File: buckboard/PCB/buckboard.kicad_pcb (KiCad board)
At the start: 2 copper layers, 387.6 x 194.6 mm, 159 parts, among them J1 Conn_01x05, SW1 SW_Push, SW10 SW_Push, SW100_1.25 SW_Push, SW101 SW_Push, SW102 SW_Push, SW103_1.25 SW_Push, SW104_1.25 SW_Push, SW105_1.25 SW_Push, SW106_1.5 SW_Push, SW11 SW_Push, SW12 SW_Push, SW13 SW_Push, SW17 SW_Push, SW18 SW_Push, SW19 SW_Push, SW2 SW_Push, SW20 SW_Push, SW21 SW_Push, SW22 SW_Push, SW23 SW_Push, SW24 SW_Push, SW25 SW_Push, SW26 SW_Push, SW27 SW_Push, SW28 SW_Push, SW29 SW_Push, SW3 SW_Push, SW30_2 SW_Push, SW4 SW_Push, SW5 SW_Push, SW58_1.5 SW_Push, SW59 SW_Push, SW6 SW_Push, SW60 SW_Push, SW61 SW_Push, SW62 SW_Push, SW63 SW_Push, SW64 SW_Push, SW65 SW_Push, SW66 SW_Push, SW67 SW_Push, SW68 SW_Push, SW69 SW_Push, SW7 SW_Push, SW70 SW_Push, SW71 SW_Push, SW71_1.75 SW_Push, SW72 SW_Push, SW73 SW_Push, SW74 SW_Push, SW75 SW_Push, SW76 SW_Push, SW77 SW_Push, SW78 SW_Push, SW79 SW_Push, SW8 SW_Push, SW80 SW_Push, SW81 SW_Push, SW82 SW_Push, SW83 SW_Push, SW84_enter1 SW_Push, SW85_1.25 SW_Push, SW86 SW_Push, SW87 SW_Push, SW88 SW_Push, SW89 SW_Push, SW9 SW_Push, SW90 SW_Push, SW91 SW_Push, SW92 SW_Push, SW93 SW_Push, SW94 SW_Push, SW95 SW_Push, SW96 SW_Push, SW97_2.75 SW_Push, SW98_1.5 SW_Push, SW99_1.25 SW_Push

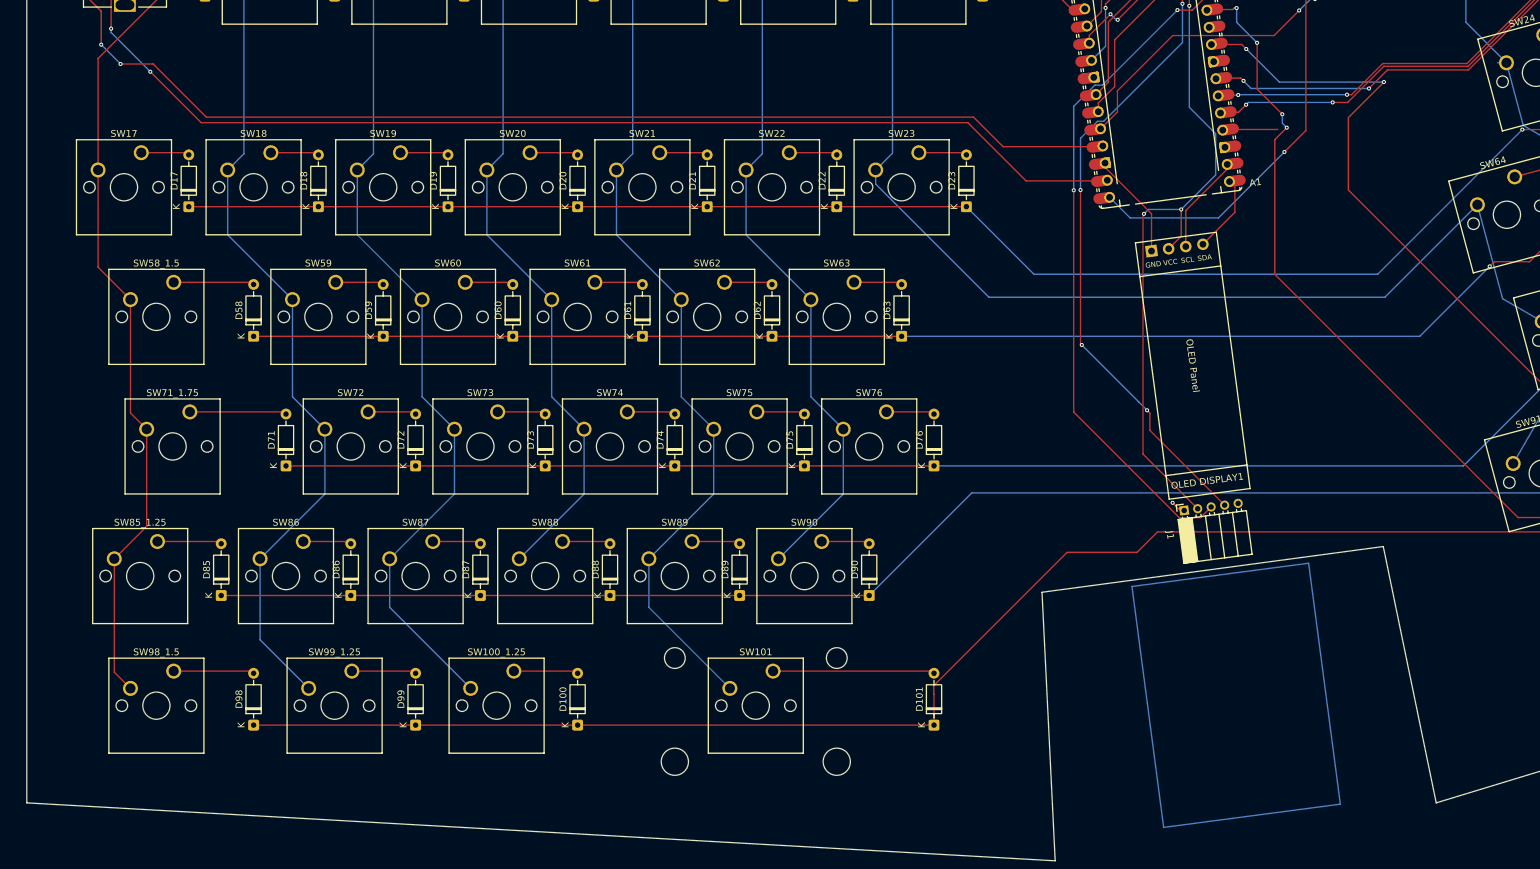
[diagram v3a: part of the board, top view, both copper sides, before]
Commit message: made working firmware for the board (joysytick still unsupported)
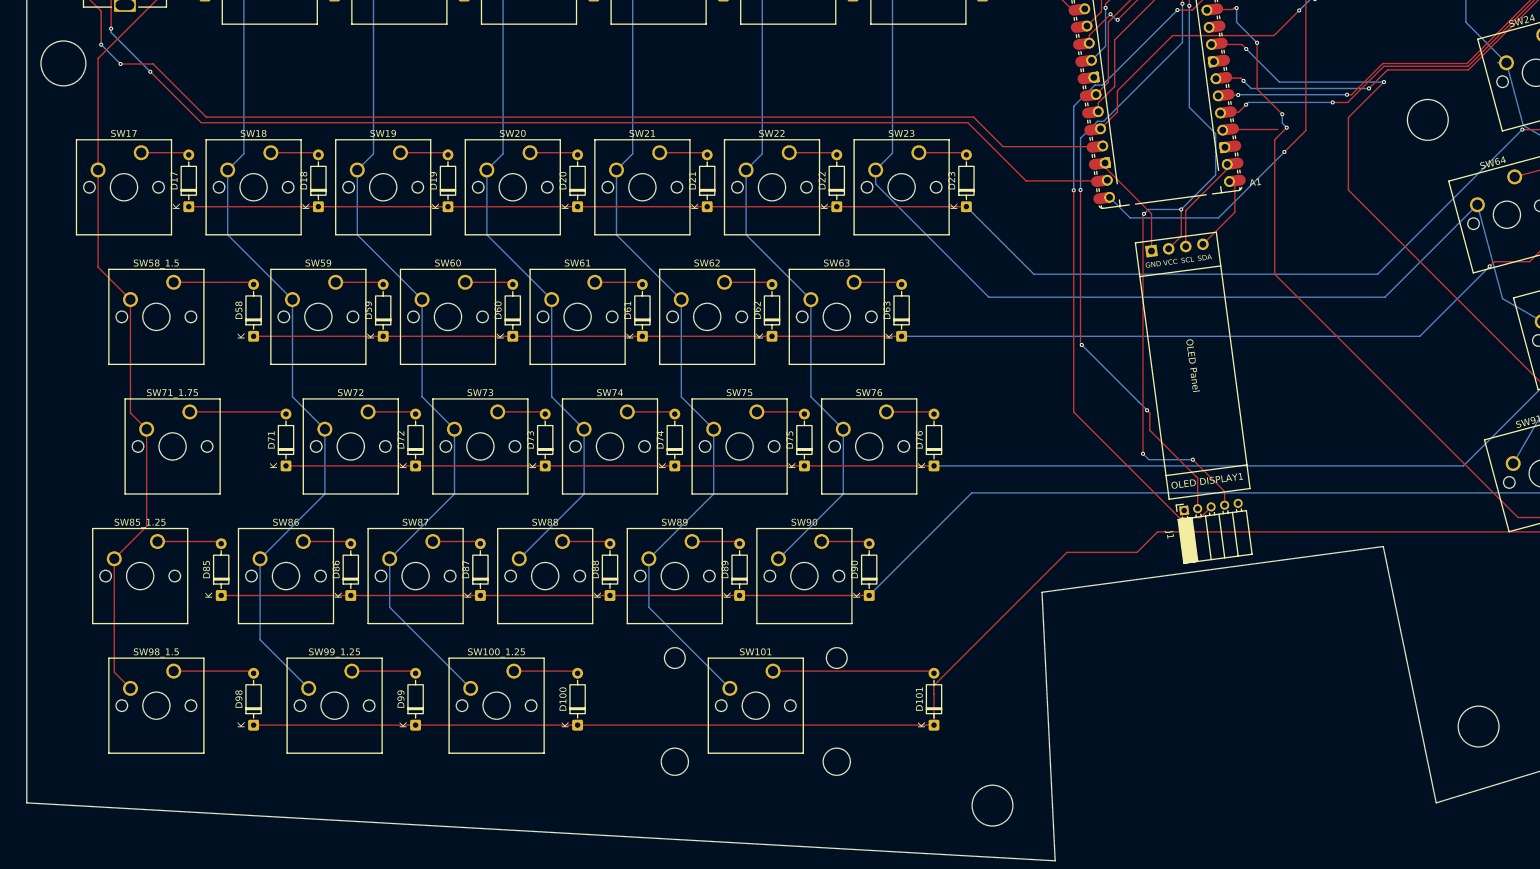
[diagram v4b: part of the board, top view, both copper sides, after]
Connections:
- J1 pad 1: GND -> JSW
- J1 pad 2: +3.3V -> VRy
- J1 pad 4: VRy -> +3.3V
- J1 pad 5: JSW -> GND
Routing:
- net +3.3V: track 109.6 -> 114.6 mm, vias 4 -> 6
- net GND: track 17.9 -> 15.8 mm, vias 1 -> 0
- net VRy: track 99.8 -> 98.6 mm
- net JSW: track 0.00 -> 0.57 mm
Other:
- outline, holes or cut-outs redrawn
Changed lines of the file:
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@@
 			(layers "*.Cu" "*.Mask")
 			(remove_unused_layers no)
-			(net "GND")
+			(net "JSW")
 			(pinfunction "Pin_1_1")
 			(pintype "passive")
@@
 			(layers "*.Cu" "*.Mask")
 			(remove_unused_layers no)
-			(net "+3.3V")
+			(net "VRy")
 			(pinfunction "Pin_2_2")
 			(pintype "passive")
@@
 			(layers "*.Cu" "*.Mask")
 			(remove_unused_layers no)
-			(net "VRy")
+			(net "+3.3V")
 			(pinfunction "Pin_4_4")
 			(pintype "passive")
@@
 			(layers "*.Cu" "*.Mask")
 			(remove_unused_layers no)
-			(net "JSW")
+			(net "GND")
 			(pinfunction "Pin_5_5")
 			(pintype "passive")
@@
 			)
 		)
+		(model "C:/Users/marin/Downloads/REDragon-MX-ZT02.stp"
+			(offset
+				(xyz -2.5 -5 0)
+			)
+			(scale
+				(xyz 1 1 1)
+			)
+			(rotate
+				(xyz -0 -0 -0)
+			)
+		)
 	)
 	(footprint "Button_Switch_Keyboard:SW_Cherry_MX_1.00u_PCB"
@@
 	(gr_poly
 		(pts
-			(xy 586.306444 230.131403) (xy 612.276103 226.712432) (xy 616.938335 262.125603) (xy 590.968676 265.544574)
+			(xy 811.498592 206.993148) (xy 631.03125 261.9375) (xy 623.25 224.26) (xy 573.088052 230.98125) (xy 575.023056 270.453588)
+			(xy 423.8625 261.9375) (xy 423.8625 126.20625) (xy 567.940824 124.087451) (xy 601.47 119.79) (xy 776.368759 75.886828)
 		)
 		(stroke
-			(width 0.2)
+			(width 0.05)
 			(type default)
 		)
 		(fill no)
-		(layer "B.Cu")
-		(net "JSW")
+		(layer "Edge.Cuts")
 	)
-	(gr_poly
-		(pts
-			(xy 811.498592 206.993148) (xy 631.03125 261.9375) (xy 623.25 224.26) (xy 573.088052 230.98125) (xy 575.023056 270.453588)
-			(xy 423.8625 261.9375) (xy 423.8625 126.20625) (xy 567.940824 124.087451) (xy 601.47 119.79) (xy 776.368759 75.886828)
+	(gr_circle
+		(center 429.249197 153.25)
+		(end 432.549197 153.25)
+		(stroke
+			(width 0.05)
+			(type solid)
+		)
+		(fill no)
+		(layer "Edge.Cuts")
+	)
+	(gr_circle
+		(center 565.81 262.34)
+		(end 568.81 262.34)
+		(stroke
+			(width 0.05)
+			(type solid)
 		)
+		(fill no)
+		(layer "Edge.Cuts")
+	)
+	(gr_circle
+		(center 629.8 161.55)
+		(end 632.8 161.55)
 		(stroke
 			(width 0.05)
-			(type default)
+			(type solid)
+		)
+		(fill no)
+		(layer "Edge.Cuts")
+	)
+	(gr_circle
+		(center 637.26 250.72)
+		(end 640.26 250.72)
+		(stroke
+			(width 0.05)
+			(type solid)
 		)
 		(fill no)
@@
 	)
 	(segment
-		(start 593.412105 218.962105)
-		(end 592.28 217.83)
-		(width 0.2)
-		(layer "F.Cu")
-		(net "GND")
-	)
-	(segment
 		(start 589.182532 175.346352)
 		(end 582.356152 168.519972)
@@
 	)
 	(segment
-		(start 593.984221 218.962105)
-		(end 593.412105 218.962105)
-		(width 0.2)
-		(layer "F.Cu")
-		(net "GND")
-	)
-	(via
-		(at 592.28 217.83)
-		(size 0.6)
-		(drill 0.3)
-		(layers "F.Cu" "B.Cu")
-		(net "GND")
-	)
-	(segment
 		(start 591.700802 180.496414)
 		(end 593.55 178.647216)
@@
 	)
 	(segment
-		(start 595.967111 218.701053)
-		(end 587.928857 210.662799)
+		(start 599.932889 218.17895)
+		(end 599.932889 216.172889)
 		(width 0.2)
 		(layer "F.Cu")
@@
 	)
 	(segment
+		(start 599.932889 216.172889)
+		(end 595.25 211.49)
+		(width 0.2)
+		(layer "F.Cu")
+		(net "+3.3V")
+	)
+	(segment
 		(start 593.42 136.26)
 		(end 594.74 137.58)
@@
 	(segment
 		(start 587.928857 210.662799)
-		(end 587.928857 175.501143)
+		(end 587.928857 210.62)
 		(width 0.2)
 		(layer "F.Cu")
@@
 		(net "+3.3V")
 	)
+	(segment
+		(start 587.928857 210.62)
+		(end 587.928857 175.501143)
+		(width 0.2)
+		(layer "F.Cu")
+		(net "+3.3V")
+	)
+	(via
+		(at 587.928857 210.62)
+		(size 0.6)
+		(drill 0.3)
+		(layers "F.Cu" "B.Cu")
+		(net "+3.3V")
+	)
 	(via
 		(at 588.07 175.36)
@@
 	)
 	(via
+		(at 595.25 211.49)
+		(size 0.6)
+		(drill 0.3)
+		(layers "F.Cu" "B.Cu")
+		(net "+3.3V")
+	)
+	(via
 		(at 593.42 133.67)
 		(size 0.6)
@@
 	)
 	(segment
+		(start 588.798857 211.49)
+		(end 587.928857 210.62)
+		(width 0.2)
+		(layer "B.Cu")
+		(net "+3.3V")
+	)
+	(segment
 		(start 596.135808 133.67)
 		(end 597.525808 132.28)
@@
 	)
 	(segment
+		(start 595.25 211.49)
+		(end 588.798857 211.49)
+		(width 0.2)
+		(layer "B.Cu")
+		(net "+3.3V")
+	)
+	(segment
 		(start 593.55 174.71)
 		(end 598.608247 169.651753)
@@
 	)
 	(segment
+		(start 595.967111 218.701053)
+		(end 595.967111 214.213171)
+		(width 0.2)
+		(layer "F.Cu")
+		(net "VRy")
+	)
+	(segment
 		(start 595.839689 137.769689)
 		(end 597.130296 137.769689)
@@
 	)
 	(segment
+		(start 595.967111 214.213171)
+		(end 595.71697 213.96303)
+		(width 0.2)
+		(layer "F.Cu")
+		(net "VRy")
+	)
+	(segment
 		(start 595.25 137.18)
 		(end 595.839689 137.769689)
@@
 	(segment
 		(start 588.94 207.186061)
-		(end 599.932889 218.17895)
+		(end 595.71697 213.96303)
 		(width 0.2)
 		(layer "F.Cu")
@@
 	)
 	(segment
+		(start 593.984221 218.962105)
+		(end 593.412105 218.962105)
+		(width 0.2)
+		(layer "F.Cu")
+		(net "JSW")
+	)
+	(segment
